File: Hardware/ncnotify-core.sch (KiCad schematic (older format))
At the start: 44 parts, among them J1 BNC5-J-P-GN-RA-BH2D, J2 Conn_ARM_JTAG_SWD_10, J3 USB4110-GF-A, Q1 NX3008NBKS, SW1 SW_Push, SW2 SW_Push, U1 STM32L422CBT6, U2 TLV71333PDBV, U3 USBLC6-2SC6, U4 USBLC6-2SC6, Y1 Q13FC1350000400

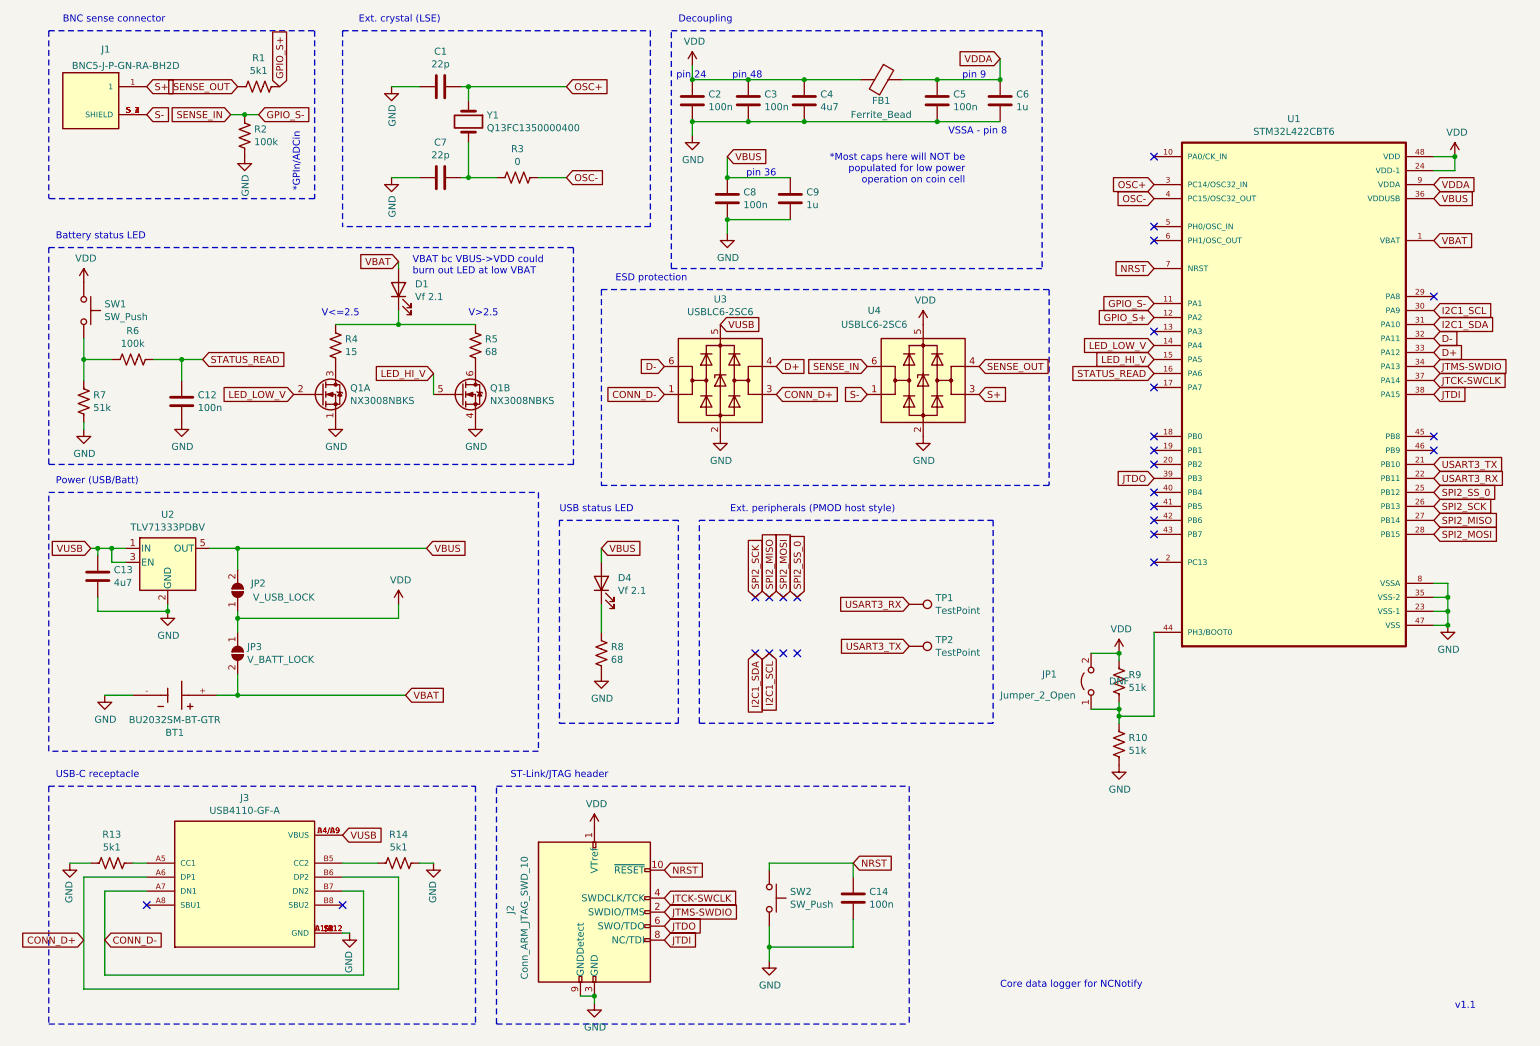
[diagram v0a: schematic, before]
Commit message: Change batt status leds; add spi/i2c test points
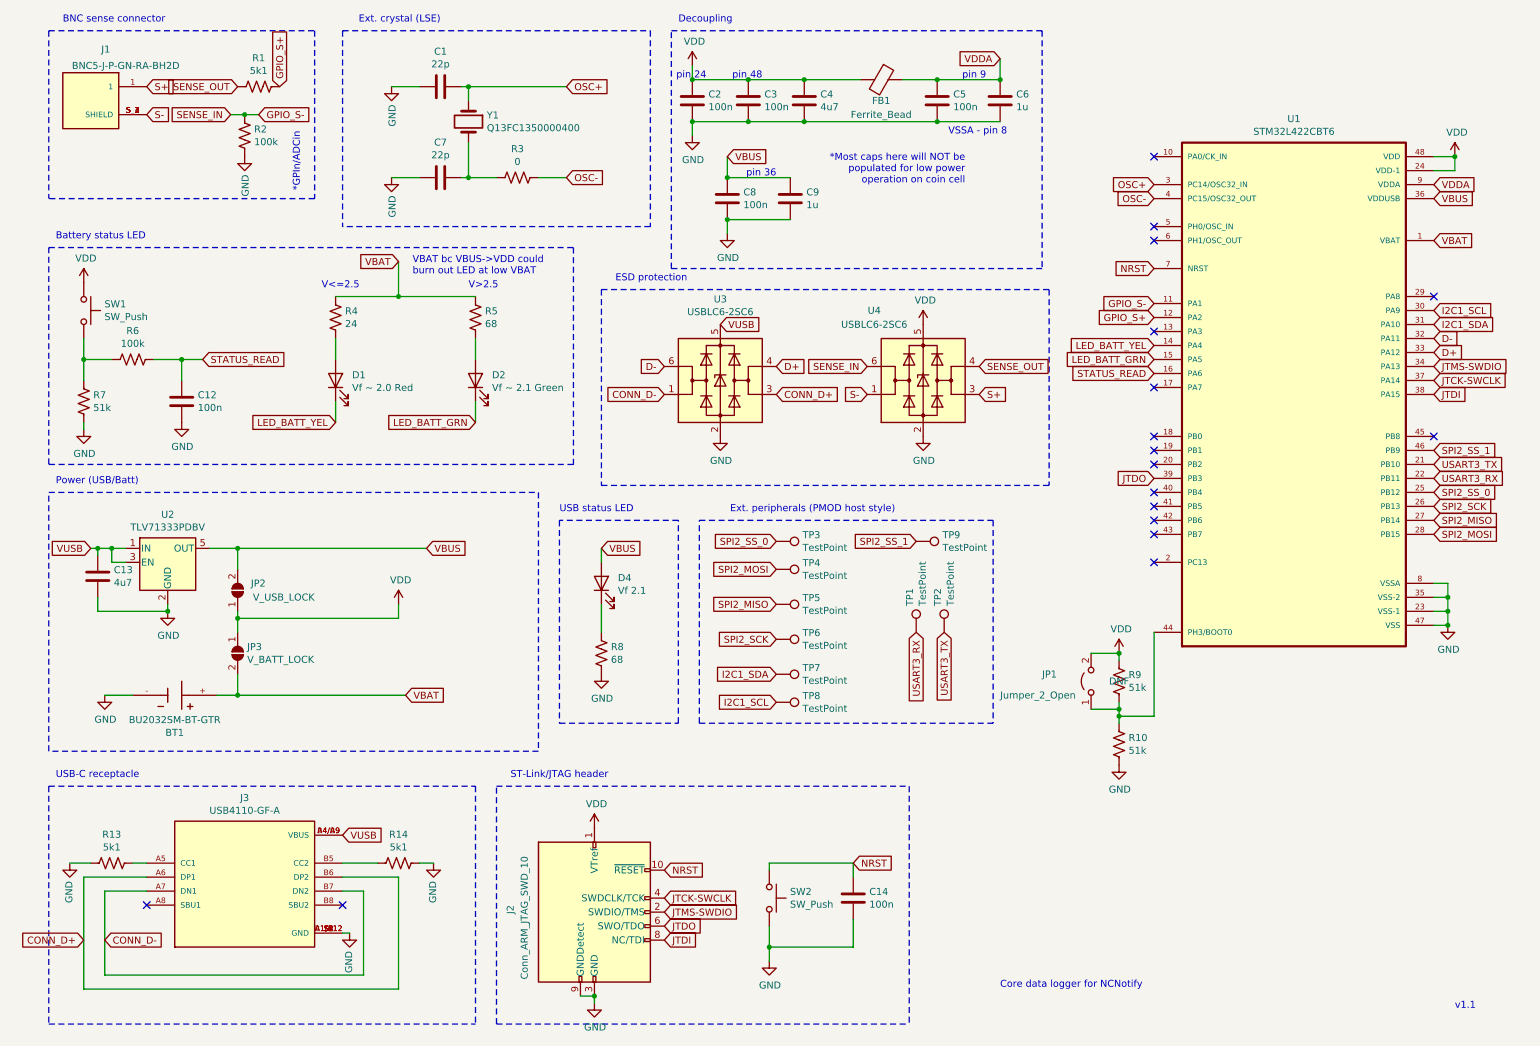
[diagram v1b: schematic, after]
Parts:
- removed Q1: NX3008NBKS, digikey-footprints:SOT-363, symbol nx3008nbks:NX3008NBKS
- added D2: Vf ~~ 2.1 Green, LED_SMD:LED_0603_1608Metric, symbol Device:LED
- added TP3, TP4, TP5, TP6, TP7, TP8, TP9: TestPoint, TestPoint:TestPoint_Pad_D1.5mm, symbol Connector:TestPoint
- D1: value Vf ~ 2.1 -> Vf ~~ 2.0 Red
- R4: value 15 -> 24
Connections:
- net I2C1_SCL: now also TP8.1
- net I2C1_SDA: now also TP7.1
- net SPI2_MISO: now also TP5.1
- net SPI2_MOSI: now also TP4.1
- net SPI2_SCK: now also TP6.1
- net SPI2_SS_0: now also TP3.1
- net VBAT: now also R4.1, R5.1; no longer D1.2 (A)
- net at R4.2: now also D1.2 (A)
- net at R5.2: now also D2.2 (A)
- net SPI2_SS_1: now reaches U1.46 (PB9)
- net SPI2_SS_1: now also TP9.1
- net LED_HI_V renamed LED_BATT_GRN
- net LED_BATT_GRN: now also D2.1 (K)
- net LED_LOW_V renamed LED_BATT_YEL
- net LED_BATT_YEL: now also D1.1 (K)
- no-connect marks 26 -> 17
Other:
- moved on the sheet: D1, R4, R5, TP1, TP2

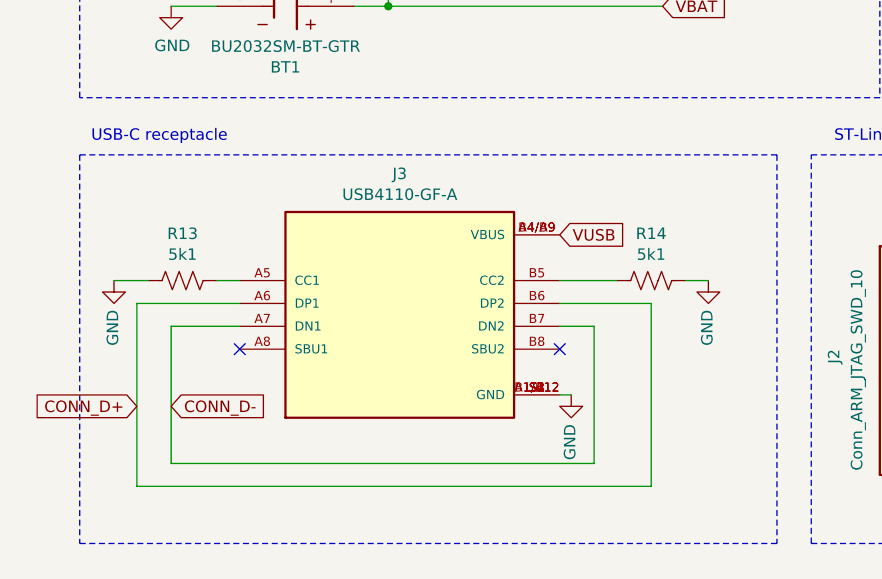
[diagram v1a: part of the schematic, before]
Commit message: swap usb port and reroute
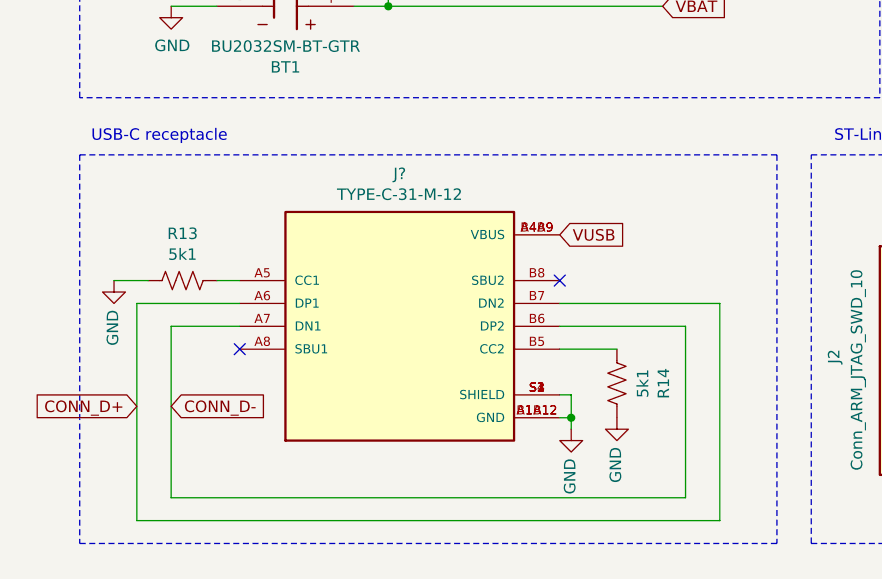
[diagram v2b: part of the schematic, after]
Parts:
- removed J3: USB4110-GF-A, libs:GCT_USB4110-GF-A, symbol USB4110-GF-A:USB4110-GF-A
- added J?: TYPE-C-31-M-12, HRO_TYPE-C-31-M-12, symbol TYPE-C-31-M-12:TYPE-C-31-M-12
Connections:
- net CONN_D+: now also J?.A6 (DP1), J?.B7 (DN2)
- net CONN_D-: now also J?.A7 (DN1), J?.B6 (DP2)
- net GND: now also J?.A1B12 (GND), J?.B1A12 (GND), J?.S1 (SHIELD), J?.S2 (SHIELD), J?.S3 (SHIELD), J?.S4 (SHIELD)
- net VUSB: now also J?.A4B9 (VBUS), J?.B4A9 (VBUS)
- net at R13.1: now also J?.A5 (CC1)
- net at R14.2: now also J?.B5 (CC2)
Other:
- moved on the sheet: R14
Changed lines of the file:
@@
 Text Notes 750  600  0    50   ~ 0
 BNC sense connector
-$Comp
-L USB4110-GF-A:USB4110-GF-A J3
-U 1 1 5FA9CA6A
-P 2050 6700
-F 0 "J3" H 2050 7267 50  0000 C CNN
-F 1 "USB4110-GF-A" H 2050 7176 50  0000 C CNN
-F 2 "libs:GCT_USB4110-GF-A" H 2050 6700 50  0001 L BNN
-F 3 "" H 2050 6700 50  0001 L BNN
-F 4 "3.26 mm" H 2050 6700 50  0001 L BNN "MAXIMUM_PACKAGE_HEIGHT"
-F 5 "A" H 2050 6700 50  0001 L BNN "PARTREV"
-F 6 "GCT" H 2050 6700 50  0001 L BNN "MANUFACTURER"
-F 7 "Manufacturer Recommendations" H 2050 6700 50  0001 L BNN "STANDARD"
-F 8 "" H 2050 6700 50  0001 C CNN "LCSC Part #"
-	1    2050 6700
-	1    0    0    -1
-$EndComp
 Text GLabel 900  7150 0    50   Input ~ 0
 CONN_D+
@@
 	1350 6800 1050 6800
 Wire Wire Line
-	1050 7400 2900 7400
-Wire Wire Line
-	900  7500 900  6700
-Wire Wire Line
 	900  6700 1350 6700
 Text GLabel 2750 6400 2    50   Input ~ 0
@@
 Wire Notes Line
 	4950 650  4950 2050
-Wire Wire Line
-	1050 6800 1050 7400
 $Comp
 L Device:R_US R14
 U 1 1 5FAA6CB5
-P 3150 6600
-F 0 "R14" V 2945 6600 50  0000 C CNN
-F 1 "5k1" V 3036 6600 50  0000 C CNN
-F 2 "Resistor_SMD:R_0402_1005Metric" V 3190 6590 50  0001 C CNN
-F 3 "~" H 3150 6600 50  0001 C CNN
-F 4 "C25905" H 3150 6600 50  0001 C CNN "LCSC Part #"
-	1    3150 6600
-	0    1    1    0
+P 3000 7050
+F 0 "R14" V 2795 7050 50  0000 C CNN
+F 1 "5k1" V 2886 7050 50  0000 C CNN
+F 2 "Resistor_SMD:R_0402_1005Metric" V 3040 7040 50  0001 C CNN
+F 3 "~" H 3000 7050 50  0001 C CNN
+F 4 "C25905" H 3000 7050 50  0001 C CNN "LCSC Part #"
+	1    3000 7050
+	-1   0    0    1
 $EndComp
 $Comp
@@
 $EndComp
 $Comp
-L power:GND #PWR028
-U 1 1 5FAA8F7D
-P 3400 6600
-F 0 "#PWR028" H 3400 6350 50  0001 C CNN
-F 1 "GND" V 3405 6472 50  0000 R CNN
-F 2 "" H 3400 6600 50  0001 C CNN
-F 3 "" H 3400 6600 50  0001 C CNN
-	1    3400 6600
-	-1   0    0    -1
-$EndComp
-$Comp
 L power:GND #PWR027
 U 1 1 5FAA933D
@@
 $EndComp
 Wire Wire Line
-	3400 6600 3300 6600
-Wire Wire Line
-	3000 6600 2750 6600
-Wire Wire Line
 	1350 6600 1250 6600
 Wire Wire Line
@@
 L power:GND #PWR029
 U 1 1 5FAA1030
-P 2800 7100
-F 0 "#PWR029" H 2800 6850 50  0001 C CNN
-F 1 "GND" V 2805 6972 50  0000 R CNN
-F 2 "" H 2800 7100 50  0001 C CNN
-F 3 "" H 2800 7100 50  0001 C CNN
-	1    2800 7100
+P 2800 7250
+F 0 "#PWR029" H 2800 7000 50  0001 C CNN
+F 1 "GND" V 2805 7122 50  0000 R CNN
+F 2 "" H 2800 7250 50  0001 C CNN
+F 3 "" H 2800 7250 50  0001 C CNN
+	1    2800 7250
 	-1   0    0    -1
 $EndComp
-NoConn ~ 2750 6900
+NoConn ~ 2750 6600
 NoConn ~ 1350 6900
 $Comp
@@
 Wire Notes Line
 	5300 5600 5300 4150
-Wire Wire Line
-	2900 6800 2750 6800
 Wire Notes Line
 	650  7750 3700 7750
@@
 Wire Notes Line
 	650  6050 650  7750
-Wire Wire Line
-	3150 6700 3150 7500
-Wire Wire Line
-	2900 6800 2900 7400
-Wire Wire Line
-	2750 6700 3150 6700
-Wire Wire Line
-	900  7500 3150 7500
 Text GLabel 5850 3050 2    50   Input ~ 0
 D+
@@
 	0    1    1    0
 $EndComp
+$Comp
+L TYPE-C-31-M-12:TYPE-C-31-M-12 J?
+U 1 1 607DA2EB
+P 2050 6800
+F 0 "J?" H 2050 7467 50  0000 C CNN
+F 1 "TYPE-C-31-M-12" H 2050 7376 50  0000 C CNN
+F 2 "HRO_TYPE-C-31-M-12" H 2050 6800 50  0001 L BNN
+F 3 "" H 2050 6800 50  0001 L BNN
+F 4 "A" H 2050 6800 50  0001 L BNN "PARTREV"
+F 5 "3.31mm" H 2050 6800 50  0001 L BNN "MAXIMUM_PACKAGE_HEIGHT"
+F 6 "Manufacturer Recommendations" H 2050 6800 50  0001 L BNN "STANDARD"
+F 7 "HRO Electronics" H 2050 6800 50  0001 L BNN "MANUFACTURER"
+	1    2050 6800
+	1    0    0    -1
+$EndComp
+Wire Wire Line
+	2750 7200 2800 7200
+Wire Wire Line
+	2800 7200 2800 7100
+Wire Wire Line
+	2800 7200 2800 7250
+Connection ~ 2800 7200
+Wire Wire Line
+	2750 6900 3000 6900
+$Comp
+L power:GND #PWR?
+U 1 1 607F7C3B
+P 3000 7200
+F 0 "#PWR?" H 3000 6950 50  0001 C CNN
+F 1 "GND" V 3005 7072 50  0000 R CNN
+F 2 "" H 3000 7200 50  0001 C CNN
+F 3 "" H 3000 7200 50  0001 C CNN
+	1    3000 7200
+	-1   0    0    -1
+$EndComp
+Wire Wire Line
+	2750 6700 3450 6700
+Wire Wire Line
+	2750 6800 3300 6800
+Wire Wire Line
+	1050 7550 3300 7550
+Wire Wire Line
+	3300 6800 3300 7550
+Wire Wire Line
+	3450 6700 3450 7650
+Wire Wire Line
+	900  7650 3450 7650
+Wire Wire Line
+	1050 6800 1050 7550
+Wire Wire Line
+	900  6700 900  7650
 $EndSCHEMATC

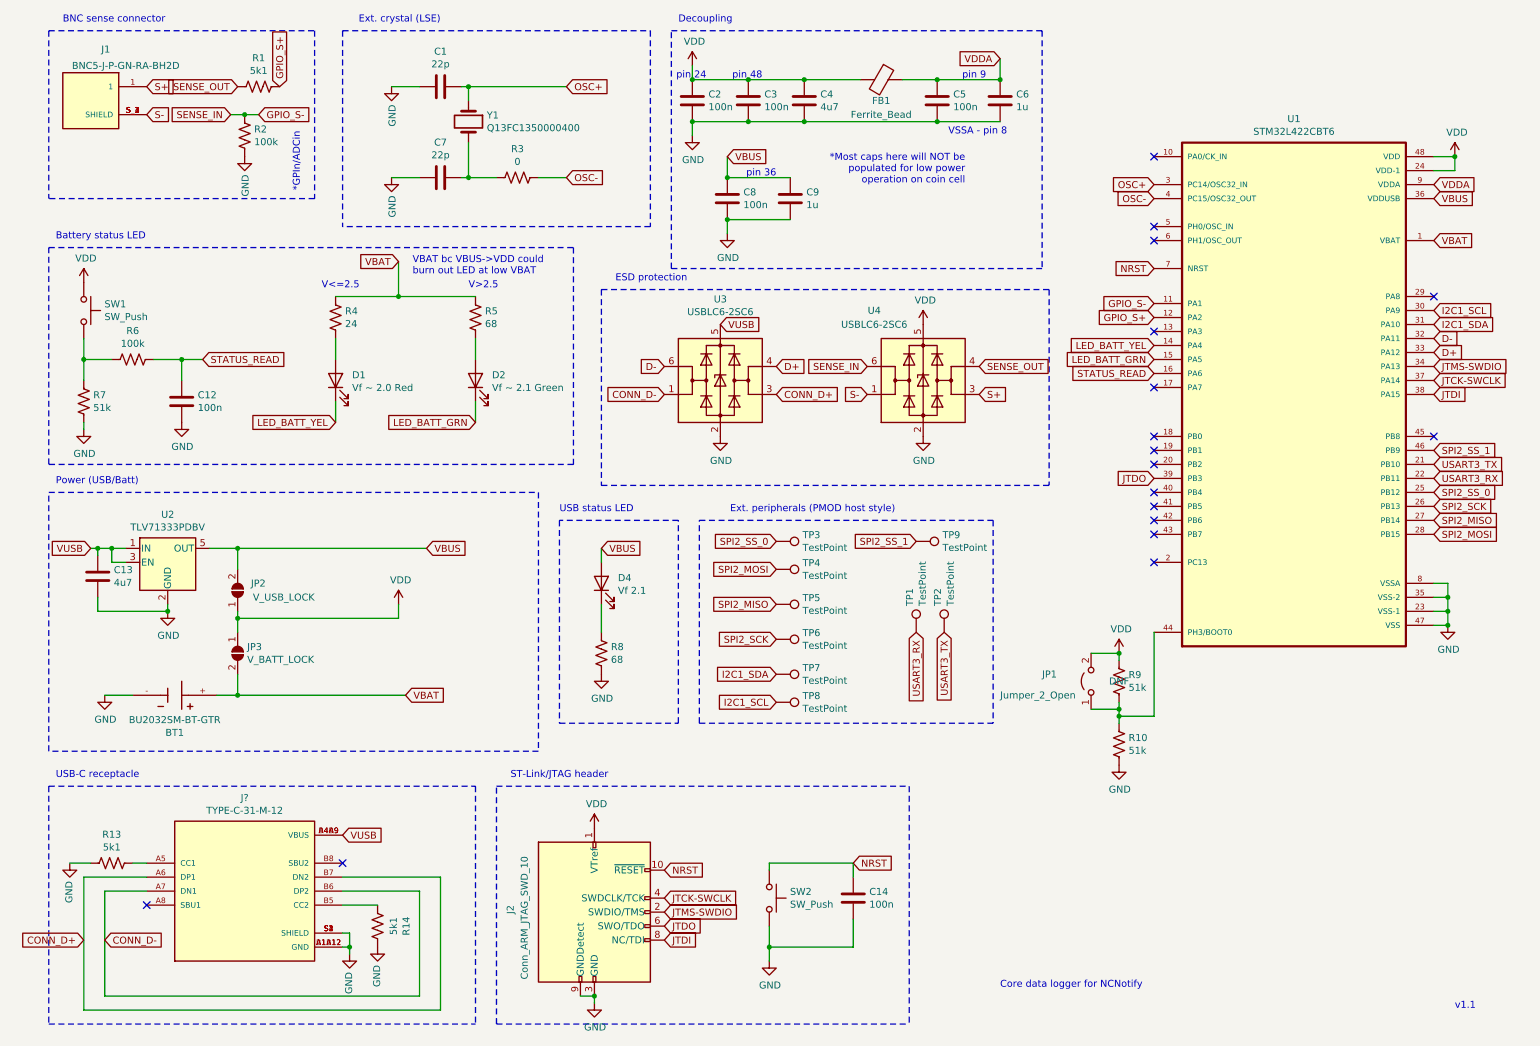
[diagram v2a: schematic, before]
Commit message: add zener option for power flexibility
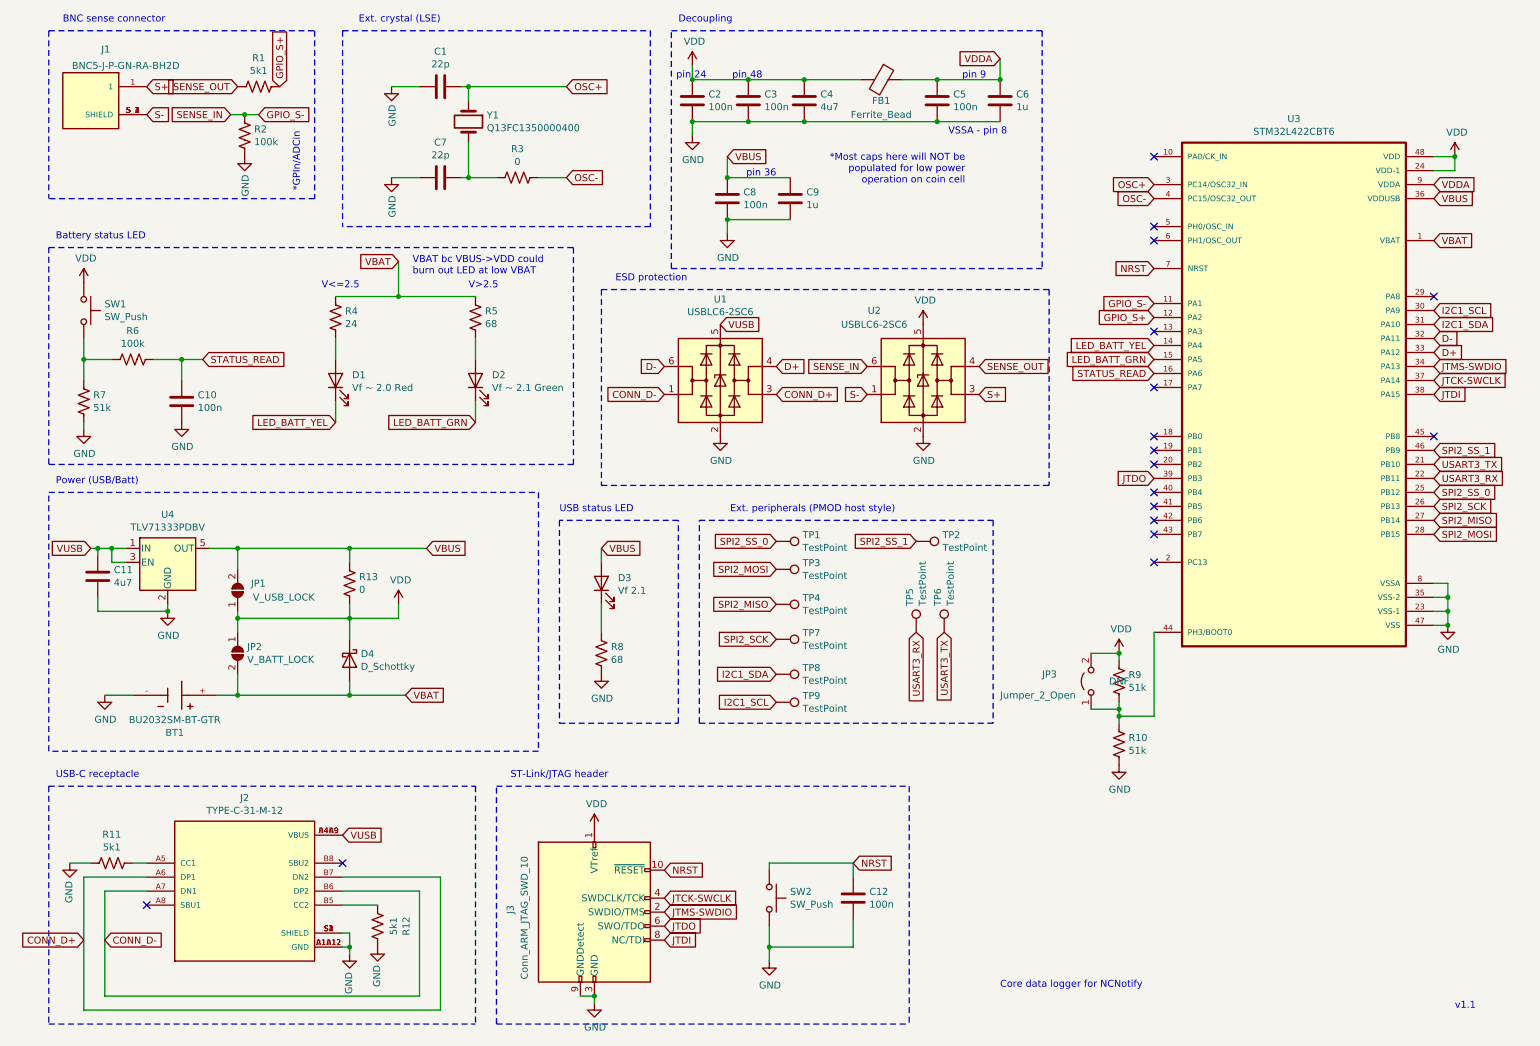
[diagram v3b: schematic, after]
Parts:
- added D4: D_Schottky, Diode_SMD:D_SOD-323, symbol Device:D_Schottky
- added R13: 0, Resistor_SMD:R_0402_1005Metric, symbol Device:R_US
- BT1: footprint BAT_BU2032SM-BT-GTR -> libs:BAT_BU2032SM-BT-GTR
- J1: footprint SAMTEC_BNC5-J-P-GN-RA-BH2D -> libs:SAMTEC_BNC5-J-P-GN-RA-BH2D
- J2: renamed from J?; footprint HRO_TYPE-C-31-M-12 -> libs:HRO_TYPE-C-31-M-12; LCSC Part # (none) -> C165948
- renumbered C12 to C10, C13 to C11, C14 to C12, D4 to D3, J2 to J3, JP2 to JP1, JP3 to JP2, JP1 to JP3, R13 to R11, R14 to R12, TP3 to TP1, TP9 to TP2, TP4 to TP3, TP5 to TP4, TP1 to TP5, TP2 to TP6, TP6 to TP7, TP7 to TP8, TP8 to TP9, U3 to U1, U4 to U2, U1 to U3, U2 to U4
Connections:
- net VBAT: now also D4.2 (A)
- net VBUS: now also R13.1
- net VDD: now also D4.1 (K), R13.2
